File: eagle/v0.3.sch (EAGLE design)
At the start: 10 parts

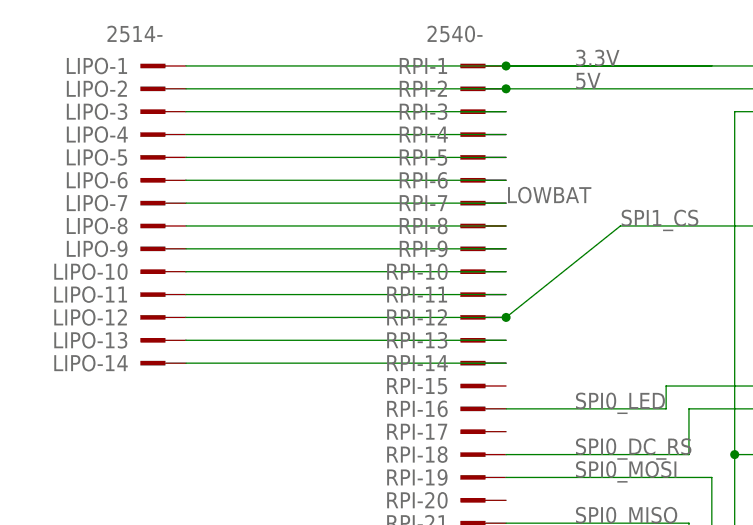
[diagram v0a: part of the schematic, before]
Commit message: Correct lipo connections.
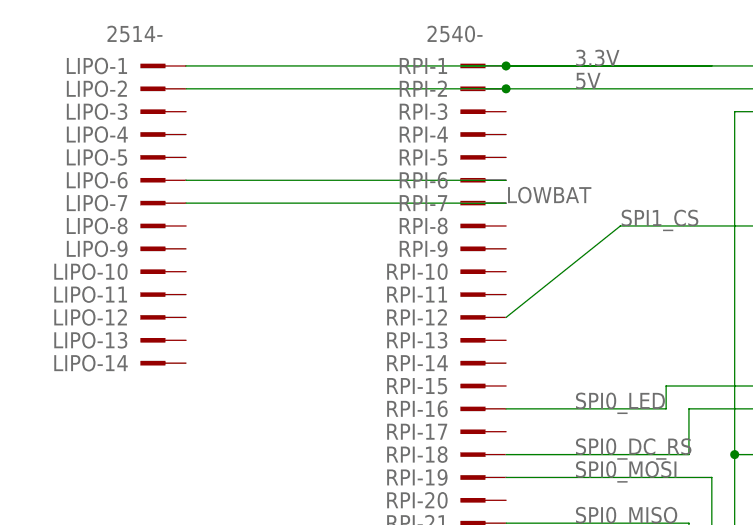
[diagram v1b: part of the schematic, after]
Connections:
- removed net N$1: LIPO-3.KL, RPI-3.KL
- removed net N$14: LIPO-14.KL, RPI-14.KL
- removed net N$2: LIPO-4.KL, RPI-4.KL
- removed net N$3: LIPO-5.KL, RPI-5.KL
- removed net N$5: LIPO-8.KL, RPI-8.KL
- removed net N$6: LIPO-9.KL, RPI-9.KL
- removed net N$7: LIPO-10.KL, RPI-10.KL
- removed net N$8: LIPO-11.KL, RPI-11.KL
- removed net N$9: LIPO-13.KL, RPI-13.KL
- net SPI1_CS: no longer LIPO-12.KL
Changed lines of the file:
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@@
 <wire x1="17.78" y1="76.2" x2="88.9" y2="76.2" width="0.1524" layer="91"/>
 <label x="17.78" y="76.2" size="1.778" layer="95"/>
-<pinref part="LIPO" gate="-12" pin="KL"/>
-<wire x1="-30.48" y1="66.04" x2="5.08" y2="66.04" width="0.1524" layer="91"/>
-<junction x="5.08" y="66.04"/>
 </segment>
 </net>
@@
 </segment>
 </net>
-<net name="N$14" class="0">
-<segment>
-<pinref part="LIPO" gate="-14" pin="KL"/>
-<pinref part="RPI" gate="-14" pin="KL"/>
-<wire x1="-30.48" y1="60.96" x2="5.08" y2="60.96" width="0.1524" layer="91"/>
-</segment>
-</net>
-<net name="N$1" class="0">
-<segment>
-<pinref part="LIPO" gate="-3" pin="KL"/>
-<pinref part="RPI" gate="-3" pin="KL"/>
-<wire x1="-30.48" y1="88.9" x2="5.08" y2="88.9" width="0.1524" layer="91"/>
-</segment>
-</net>
-<net name="N$2" class="0">
-<segment>
-<pinref part="RPI" gate="-4" pin="KL"/>
-<pinref part="LIPO" gate="-4" pin="KL"/>
-<wire x1="5.08" y1="86.36" x2="-30.48" y2="86.36" width="0.1524" layer="91"/>
-</segment>
-</net>
-<net name="N$3" class="0">
-<segment>
-<pinref part="LIPO" gate="-5" pin="KL"/>
-<pinref part="RPI" gate="-5" pin="KL"/>
-<wire x1="-30.48" y1="83.82" x2="5.08" y2="83.82" width="0.1524" layer="91"/>
-</segment>
-</net>
 <net name="N$4" class="0">
 <segment>
@@
 </segment>
 </net>
-<net name="N$5" class="0">
-<segment>
-<pinref part="LIPO" gate="-8" pin="KL"/>
-<pinref part="RPI" gate="-8" pin="KL"/>
-<wire x1="-30.48" y1="76.2" x2="5.08" y2="76.2" width="0.1524" layer="91"/>
-</segment>
-</net>
-<net name="N$6" class="0">
-<segment>
-<pinref part="RPI" gate="-9" pin="KL"/>
-<pinref part="LIPO" gate="-9" pin="KL"/>
-<wire x1="5.08" y1="73.66" x2="-30.48" y2="73.66" width="0.1524" layer="91"/>
-</segment>
-</net>
-<net name="N$7" class="0">
-<segment>
-<pinref part="LIPO" gate="-10" pin="KL"/>
-<pinref part="RPI" gate="-10" pin="KL"/>
-<wire x1="-30.48" y1="71.12" x2="5.08" y2="71.12" width="0.1524" layer="91"/>
-</segment>
-</net>
-<net name="N$8" class="0">
-<segment>
-<pinref part="RPI" gate="-11" pin="KL"/>
-<pinref part="LIPO" gate="-11" pin="KL"/>
-<wire x1="5.08" y1="68.58" x2="-30.48" y2="68.58" width="0.1524" layer="91"/>
-</segment>
-</net>
-<net name="N$9" class="0">
-<segment>
-<pinref part="RPI" gate="-13" pin="KL"/>
-<pinref part="LIPO" gate="-13" pin="KL"/>
-<wire x1="5.08" y1="63.5" x2="-30.48" y2="63.5" width="0.1524" layer="91"/>
-</segment>
-</net>
